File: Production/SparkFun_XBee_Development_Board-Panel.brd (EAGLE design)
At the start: 198.1 x 158.2 mm, 1094 parts, among them J1 USB Female Type C Connector, J13 QWIIC_RIGHT_ANGLE, J14 USB Female Type C Connector, J17 USB Female Type C Connector, J23 QWIIC_RIGHT_ANGLE, J24 USB Female Type C Connector, J27 USB Female Type C Connector, J3 USB Female Type C Connector, J33 QWIIC_RIGHT_ANGLE, J34 USB Female Type C Connector, J37 USB Female Type C Connector, J4 QWIIC_RIGHT_ANGLE, J43 QWIIC_RIGHT_ANGLE, J44 USB Female Type C Connector, J47 USB Female Type C Connector, J53 QWIIC_RIGHT_ANGLE, J54 USB Female Type C Connector, J57 USB Female Type C Connector, J63 QWIIC_RIGHT_ANGLE, J64 USB Female Type C Connector, J67 USB Female Type C Connector, J73 QWIIC_RIGHT_ANGLE, J74 USB Female Type C Connector, J77 USB Female Type C Connector, Q1 3.1A/30V/105mΩ, Q2 3.1A/30V/105mΩ, Q3 3.1A/30V/105mΩ, Q4 3.1A/30V/105mΩ, Q5 3.1A/30V/105mΩ, Q6 3.1A/30V/105mΩ, Q7 3.1A/30V/105mΩ, Q8 3.1A/30V/105mΩ, U1 FSUSB30MUX_MSOP10, U10 FT231XS, U11 FSUSB30MUX_MSOP10, U12 AP63203, U13 ESD Diode, U14 ESD Diode, U15 FT231XS, U16 FSUSB30MUX_MSOP10, U17 AP63203, U18 ESD Diode, U19 ESD Diode, U2 AP63203, U20 FT231XS, U21 FSUSB30MUX_MSOP10, U22 AP63203, U23 ESD Diode, U24 ESD Diode, U25 FT231XS, U26 FSUSB30MUX_MSOP10, U27 AP63203, U28 ESD Diode, U29 ESD Diode, U3 ESD Diode, U30 FT231XS, U31 FSUSB30MUX_MSOP10, U32 AP63203, U33 ESD Diode, U34 ESD Diode, U35 FT231XS, U36 FSUSB30MUX_MSOP10, U37 AP63203, U38 ESD Diode, U39 ESD Diode, U4 FSUSB30MUX_MSOP10, U40 FT231XS, U5 ESD Diode, U6 AP63203, U7 FT231XS, U8 ESD Diode, U9 ESD Diode

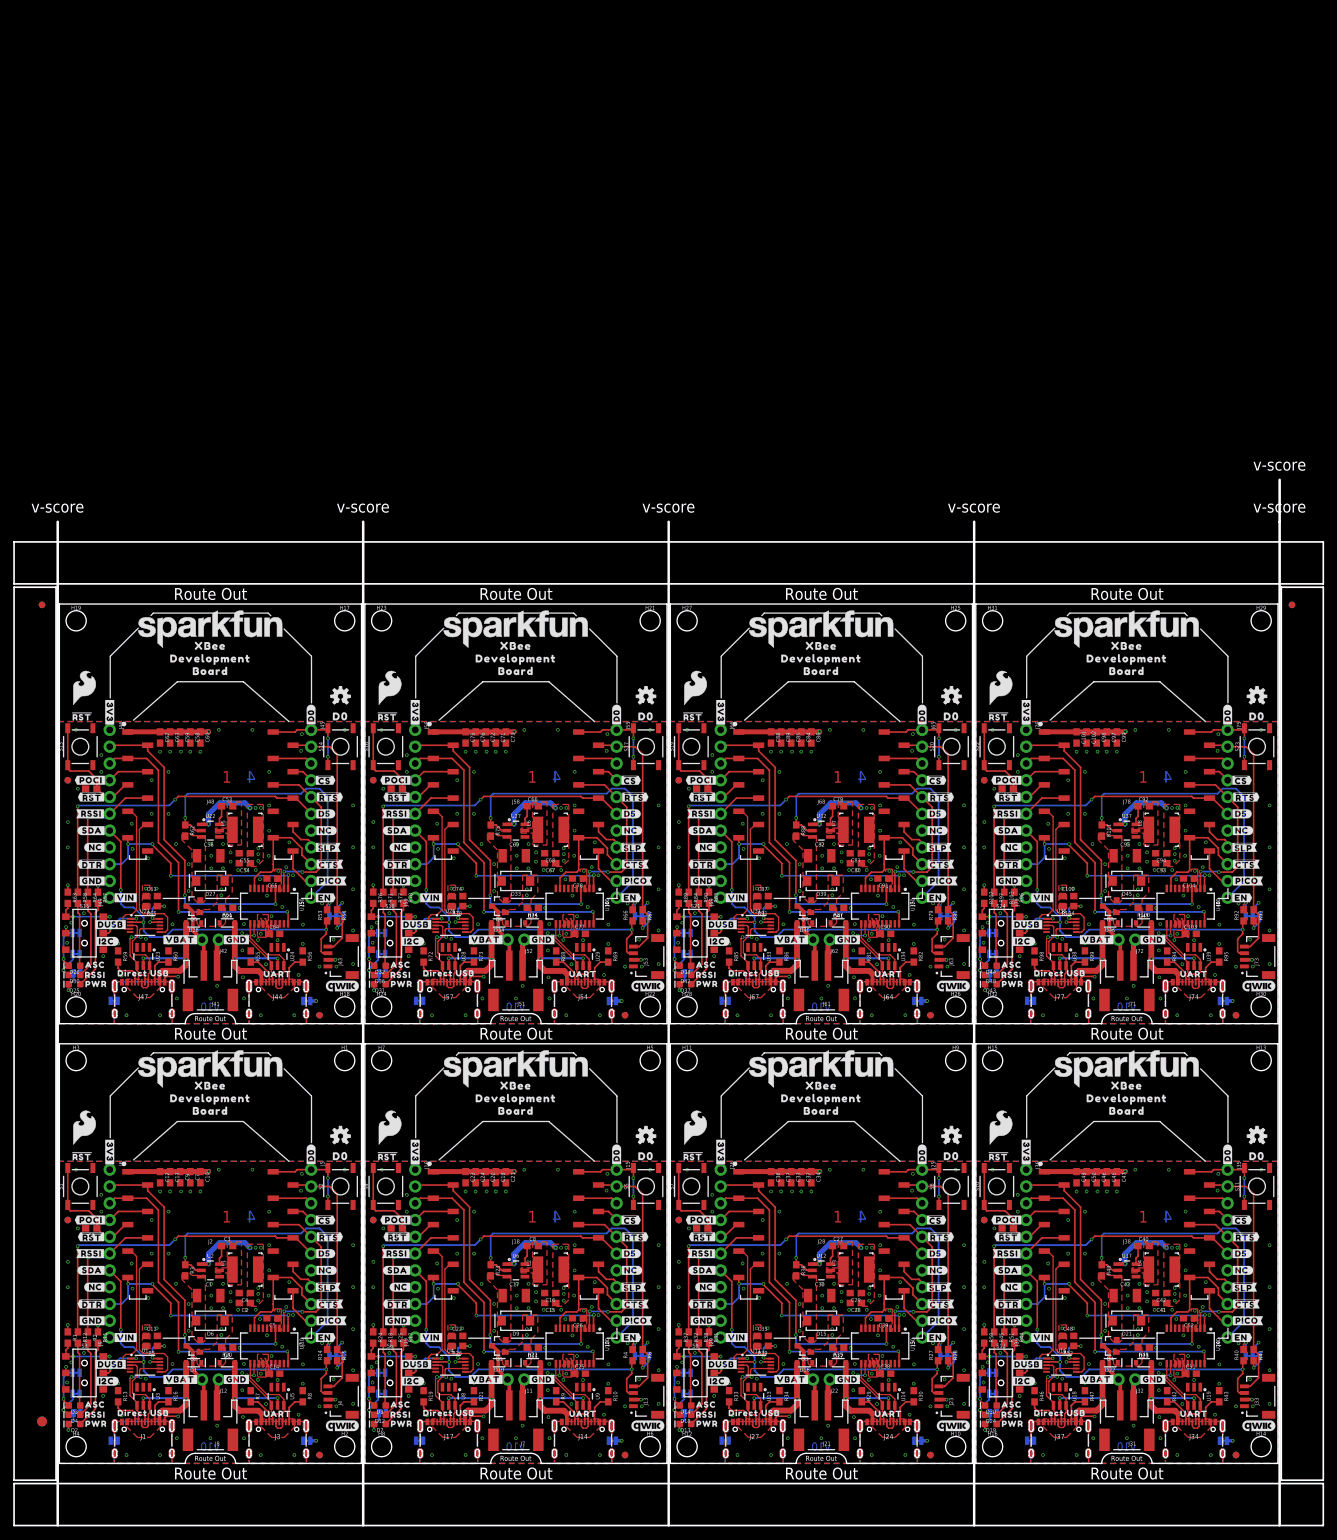
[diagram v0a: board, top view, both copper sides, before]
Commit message: Adds new 2 x 3 panel
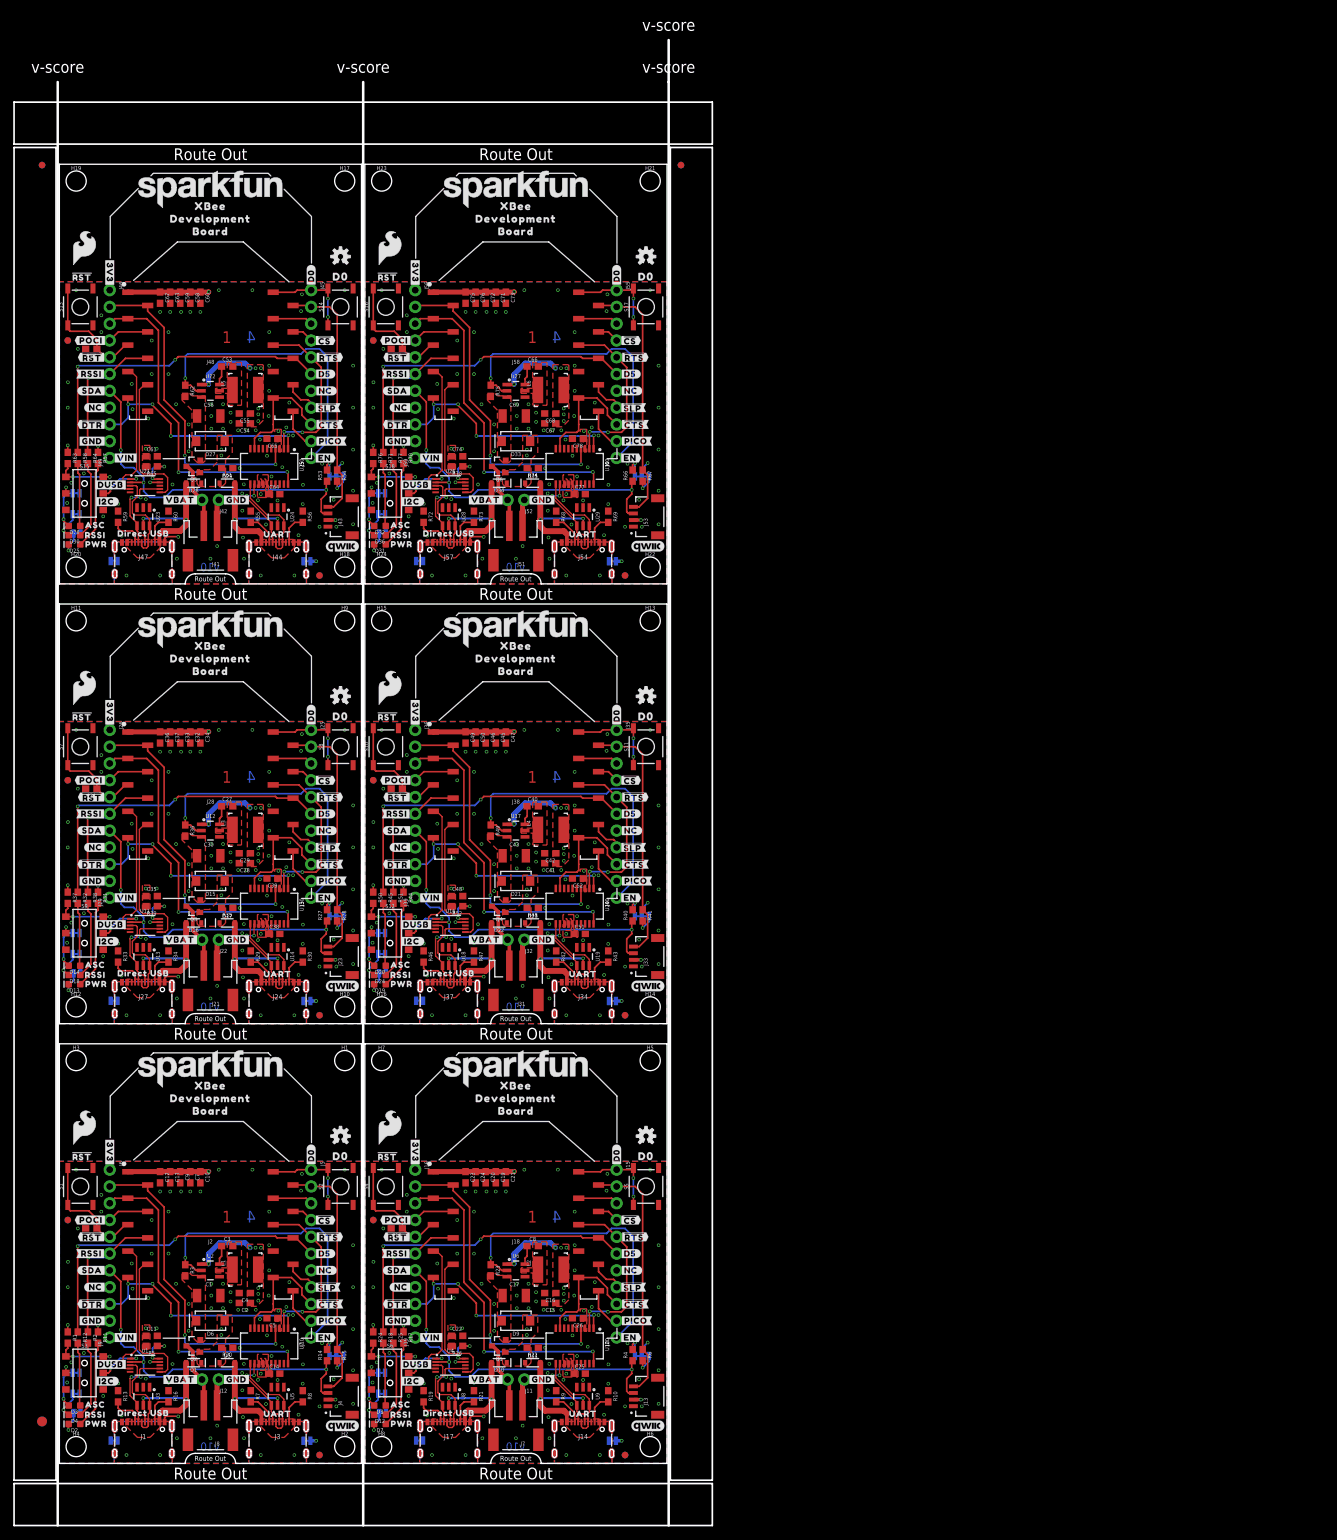
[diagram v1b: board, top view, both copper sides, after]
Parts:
- removed ALED6, ALED7, PLED6, PLED7, RLED6, RLED7, SHLD12, SHLD13, SHLD14, SHLD15: JUMPER-SMT_2_NC_TRACE_SILK, SparkFun-Jumpers:SMT-JUMPER_2_NC_TRACE_SILK
- removed C100, C103, C104, C79, C85, C87, C90, C91, C92, C98: 0.1uF, SparkFun-Capacitors:0603
- removed C101, C88: 10pF, SparkFun-Capacitors:0603
- removed C102, C89: 47pF, SparkFun-Capacitors:0603
- removed C80, C81, C93, C94: 22uF, SparkFun-Capacitors:0603
- removed C82, C95: 10uF, SparkFun-Capacitors:1210
- removed C83, C84, C96, C97: 10nF, SparkFun-Capacitors:0603
- removed C86, C99: 10uF, SparkFun-Capacitors:0603
- removed D37, D43: RED, SparkFun-LED:LED-0603
- removed D38, D44: BLUE, SparkFun-LED:LED-0603
- removed D39, D45: 3A/40V/500mV, SparkFun-DiscreteSemi:SMA-DIODE
- removed D40, D41, D46, D47: 3A/10V/280mV, SparkFun-DiscreteSemi:SOD-323
- removed D42, D48: Yellow, SparkFun-LED:LED-0603
- removed FD25, FD26, FD27, FD28, FD29, FD30, FD31, FD32: FIDUCIAL1X2, SparkFun-Aesthetics:FIDUCIAL-1X2
- removed H25, H26, H27, H28, H29, H30, H31, H32: STAND-OFFTIGHT, SparkFun-Hardware:STAND-OFF-TIGHT
- removed I2C_PU6, I2C_PU7: JUMPER-SMT_3_2-NC_TRACE_SILK, SparkFun-Jumpers:SMT-JUMPER_3_2-NC_TRACE_SILK
- removed J61, J71: (no value), SparkFun-Connectors:JST-2-SMD
- removed J62, J72: (no value), SparkFun-Connectors:1X02_NO_SILK
- removed J63, J73: QWIIC_RIGHT_ANGLE, SparkFun-Connectors:JST04_1MM_RA
- removed J64, J67, J74, J77: USB Female Type C Connector, SparkFun-Connectors:USB-C-16P-4LAYER-ISOLATED
- removed J65, J66, J75, J76: (no value), SparkFun-Connectors:1X10_NO_SILK
- removed J68, J78: (no value), xbee_smart_modem:XBEE3-SMD
- removed J69, J70, J79, J80: (no value), SparkFun-Connectors:1X01_NO_SILK_STAND
- removed L7, L8: 3.9UH, SparkFun-Coils:INDUCTOR_3.9UH
- removed LOGO19, LOGO22: OSHW-LOGOS, SparkFun-Aesthetics:OSHW-LOGO-S
- removed LOGO20, LOGO23: QWIIC_LOGO_5MM, SparkFun-Aesthetics:QWIIC_5MM
- removed LOGO21, LOGO24: SFE_LOGO_NAME.2_INCH, SparkFun-Aesthetics:SFE_LOGO_NAME_.2
- removed Q7, Q8: 3.1A/30V/105mΩ, SparkFun-DiscreteSemi:SOT23-3
- removed R100, R101, R87, R88: 10k, SparkFun-Resistors:0603
- removed R102, R89: 100k, SparkFun-Resistors:0603
- removed R103, R79, R80, R84, R90, R92, R93, R97: 2.2k, SparkFun-Resistors:0603
- removed R104, R91: 100, SparkFun-Resistors:0603
- removed R81, R82, R85, R86, R94, R95, R98, R99: 5.1k, SparkFun-Resistors:0603
- removed R83, R96: 1k, SparkFun-Resistors:0603
- removed S19, S20, S22, S23: (no value), SparkFun-Switches:TACTILE_SWITCH_SMD_5.2MM
- removed S21, S24: (no value), SparkFun-Switches:SWITCH_DPDT_SMD_AYZ0202
- removed U$403, U$470: (no value), top:##CS##19
- removed U$404, U$471: (no value), top:##CTS##25
- removed U$405, U$472: (no value), top:##RTS##24
- removed U$406, U$419, U$473, U$486: (no value), top:#3V3#1
- removed U$407, U$474: (no value), top:#D0#18
- removed U$408, U$415, U$420, U$442, U$475, U$482, U$487, U$509: (no value), top:#GND#0
- removed U$409, U$476: (no value), top:#I2C#33
- removed U$410, U$477: (no value), top:#PICO#23
- removed U$411, U$478: (no value), top:#RSSI#16
- removed U$412, U$479: (no value), top:#SDA#7
- removed U$413, U$480: (no value), top:#SHLD#30
- removed U$414, U$481: (no value), top:#SHLD1#31
- removed U$416, U$483: (no value), bot:#D5#3
- removed U$417, U$421, U$484, U$488: (no value), top:#VIN#4
- removed U$418, U$485: (no value), top:PWR26
- removed U$422, U$489: (no value), top:##SLP##27
- removed U$423, U$490: (no value), bot:#I2C#31
- removed U$424, U$491: (no value), bot:D03
- removed U$425, U$438, U$492, U$505: (no value), top:##RST##15
- removed U$426, U$441, U$493, U$508: (no value), top:#VBAT#5
- removed U$427, U$494: (no value), top:#ALED#21
- removed U$428, U$495: (no value), top:#PLED#20
- removed U$429, U$496: (no value), top:#D0#AD0#18
- removed U$430, U$497: (no value), top:#D3#AD3#22
- removed U$431, U$498: (no value), top:#D4#PICO#24
- removed U$432, U$499: (no value), top:#D5#ASSOC#24
- removed U$433, U$500: (no value), top:#D6##RTS##24
- removed U$434, U$501: (no value), top:#D7##CTS##25
- removed U$435, U$502: (no value), top:#D9##SLP##27
- removed U$436, U$503: (no value), top:#TXO#D13#13
- removed U$437, U$504: (no value), top:#RXI#D14#15
- removed U$439, U$506: (no value), top:#RSSI#D10#17
- removed U$440, U$507: (no value), top:#SDA#D11#8
- removed U$443, U$510: (no value), top:UART32
- removed U$444, U$511: (no value), top:#RST#30
- removed U$445, U$512: (no value), SparkFun-Aesthetics:SFE_LOGO_NAME_.2
- removed U$446, U$513: (no value), SparkFun-Aesthetics:SFE_LOGO_FLAME_.2
- removed U$447, U$514: (no value), top:RSSI31
- removed U$448, U$515: (no value), top:#RLED#22
- removed U$449, U$516: (no value), top:#POCI#D12#24
- removed U$450, U$517: (no value), top:#POCI#23
- removed U$451, U$518: (no value), top:##DTR##27
- removed U$452, U$453, U$519, U$520: (no value), topmirror:#EN#17
- removed U$454, U$457, U$521, U$524: (no value), topmirror:#NC#1
- removed U$455, U$456, U$522, U$523: (no value), botmirror:#NC#3
- removed U$458, U$525: (no value), topmirror:DIRECT_USB33
- removed U$459, U$461, U$526, U$528: (no value), topmirror:DEVELOPMENT1345
- removed U$460, U$462, U$527, U$529: (no value), topmirror:BOARD1346
- removed U$463, U$530: (no value), botmirror:#DUSB#31
- removed U$464, U$465, U$531, U$532: (no value), top:XBEE339
- removed U$466, U$533: (no value), top:#D1#AD1#SCL#8
- removed U$467, U$534: (no value), top:#D8##DTR##27
- removed U$468, U$535: (no value), top:ASC32
- removed U$469, U$536: (no value), top:#D2#AD2#SCLK#19
- removed U31, U36: FSUSB30MUX_MSOP10, SparkFun-IC-Special-Function:MSOP10
- removed U32, U37: AP63203, SparkFun-IC-Power:SOT23-6
- removed U33, U34, U38, U39: ESD Diode, SparkFun-DiscreteSemi:SOT-23-6
- removed U35, U40: FT231XS, SparkFun-IC-Comms:SSOP20_L
- moved C47 113.9 mm to (67.6, 109.9)
- moved C50 113.9 mm to (63.0, 109.9)
- moved D21 113.9 mm to (69.1, 88.1)
- moved E$3 113.9 mm to (94.1, 196.5)
- moved E$4 113.9 mm to (94.1, 196.5)
- moved FD13 113.9 mm to (47.5, 103.4)
- moved FD14 113.9 mm to (47.5, 103.4)
- moved I2C_PU2 113.9 mm to (41.9, 82.8)
- moved J25 113.9 mm to (38.1, 111.0)
- moved J30 113.9 mm to (38.1, 85.6)
- moved J31 113.9 mm to (69.1, 71.6)
- moved J33 113.9 mm to (86.9, 76.7)
- moved J38 113.9 mm to (69.1, 99.6)
- moved LOGO10 113.9 mm to (88.8, 116.1)
- moved LOGO12 113.9 mm to (69.1, 126.2)
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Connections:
- removed net !RESET!6: C83.1, J66.5, J68.5, S19.1, S19.2
- removed net !RESET!7: C96.1, J76.5, J78.5, S22.1, S22.2
- removed net 3.3V6: C80.1, C81.1, C84.1, C85.1, C86.1, C87.1, C88.1, C89.1, C90.1, C91.1, I2C_PU6.2, J63.2, J66.1, J68.1, L7.P$2, R83.1, R89.1, R91.2, U32.1, U35.13, U35.14, U35.15, U35.3
- removed net 3.3V7: C100.1, C101.1, C102.1, C103.1, C104.1, C93.1, C94.1, C97.1, C98.1, C99.1, I2C_PU7.2, J73.2, J76.1, J78.1, L8.P$2, R102.1, R104.2, R96.1, U37.1, U40.13, U40.14, U40.15, U40.3
- removed net ALED6: ALED6.2, D38.C
- removed net ALED7: ALED7.2, D44.C
- removed net D+6: J64.A6, J64.B6, U34.6, U35.11
- removed net D+7: J74.A6, J74.B6, U39.6, U40.11
- removed net D-6: J64.A7, J64.B7, U34.4, U35.12
- removed net D-7: J74.A7, J74.B7, U39.4, U40.12
- removed net D1/SCL6: J63.4, J65.2, J68.19, R80.1
- removed net D1/SCL7: J73.4, J75.2, J78.19, R93.1
- removed net D10/RSSI_PWM6: J66.6, J68.6, R90.1
- removed net D10/RSSI_PWM7: J76.6, J78.6, R103.1
- removed net D11/SDA6: J63.3, J66.7, R79.1, U31.2
- removed net D11/SDA7: J73.3, J76.7, R92.1, U36.2
- removed net D12/SPI_POCI6: J66.4, J68.4
- removed net D12/SPI_POCI7: J76.4, J78.4
- removed net D13/TXO6: J66.2, J68.2, U35.4
- removed net D13/TXO7: J76.2, J78.2, U40.4
- removed net D14/RXI6: J66.3, J68.3, U35.20
- removed net D14/RXI7: J76.3, J78.3, U40.20
- removed net D2/SPI_CLK6: J65.3, J68.18
- removed net D2/SPI_CLK7: J75.3, J78.18
- removed net D3/SPI_!CS!6: J65.4, J68.17
- removed net D3/SPI_!CS!7: J75.4, J78.17
- removed net D4/SPI_PICO6: J65.10, J68.11
- removed net D4/SPI_PICO7: J75.10, J78.11
- removed net D5/ASSOCIATE6: J65.6, J68.15, R84.1
- removed net D5/ASSOCIATE7: J75.6, J78.15, R97.1
- removed net D6: J65.1, J68.20, S20.1, S20.2
- removed net D6/!RTS!6: J65.5, J68.16, U35.2
- removed net D6/!RTS!7: J75.5, J78.16, U40.2
- removed net D7: J75.1, J78.20, S23.1, S23.2
- removed net D7/!CTS!6: J65.9, J68.12, U35.9
- removed net D7/!CTS!7: J75.9, J78.12, U40.9
- removed net D8/!DTR!6: J66.9, J68.9, U35.1
- removed net D8/!DTR!7: J76.9, J78.9, U40.1
- removed net D9/!SLEEP!6: J65.8, J68.13
- removed net D9/!SLEEP!7: J75.8, J78.13
- removed net DIRECT_D+6: J67.A6, J67.B6, U31.3, U33.6
- removed net DIRECT_D+7: J77.A6, J77.B6, U36.3, U38.6
- removed net DIRECT_D-6: J67.A7, J67.B7, U31.7, U33.4
- removed net DIRECT_D-7: J77.A7, J77.B7, U36.7, U38.4
- removed net DIRECT_SELECT6: S21.2, S21.5, U31.1
- removed net DIRECT_SELECT7: S24.2, S24.5, U36.1
- removed net EN6: J70.1, R88.1, U32.2
- removed net EN7: J80.1, R101.1, U37.2
- removed net FIRMWARE6: R89.2, S21.1, S21.4
- removed net FIRMWARE7: R102.2, S24.1, S24.4
- removed net GND6: ALED6.1, C80.2, C81.2, C82.2, C83.2, C84.2, C85.2, C86.2, C87.2, C88.2, C89.2, C90.2, C91.2, J61.1, J62.1, J63.1, J64.GND, J64.GND2, J66.10, J67.GND, J67.GND2, J68.10, PLED6.1, R81.1, R82.1, R85.1, R86.1, R87.1, RLED6.1, S19.3, S19.4, S20.3, S20.4, S21.3, S21.6, SHLD12.1, SHLD13.1, U31.5, U31.9, U32.4, U33.2, U34.2, U35.16, U35.6
- removed net GND7: ALED7.1, C100.2, C101.2, C102.2, C103.2, C104.2, C93.2, C94.2, C95.2, C96.2, C97.2, C98.2, C99.2, J71.1, J72.1, J73.1, J74.GND, J74.GND2, J76.10, J77.GND, J77.GND2, J78.10, PLED7.1, R100.1, R94.1, R95.1, R98.1, R99.1, RLED7.1, S22.3, S22.4, S23.3, S23.4, S24.3, S24.6, SHLD14.1, SHLD15.1, U36.5, U36.9, U37.4, U38.2, U39.2, U40.16, U40.6
- removed net N$100: C95.1, D45.C, Q8.2, R101.2, U37.3
- removed net N$101: C92.1, U37.6
- removed net N$102: C92.2, L8.P$1, U37.5
- removed net N$103: D48.A, R103.2
- removed net N$104: R104.1, U36.10
- removed net N$79: I2C_PU6.3, R79.2
- removed net N$80: I2C_PU6.1, R80.2
- removed net N$81: J64.B5, R82.2
- removed net N$82: J64.A5, R81.2
- removed net N$83: D37.A, R83.2
- removed net N$84: D38.A, R84.2
- removed net N$85: J67.B5, R86.2
- removed net N$86: J67.A5, R85.2
- removed net N$87: C82.1, D39.C, Q7.2, R88.2, U32.3
- removed net N$88: C79.1, U32.6
- removed net N$89: C79.2, L7.P$1, U32.5
- removed net N$90: D42.A, R90.2
- removed net N$91: R91.1, U31.10
- removed net N$92: I2C_PU7.3, R92.2
- removed net N$93: I2C_PU7.1, R93.2
- removed net N$94: J74.B5, R95.2
- removed net N$95: J74.A5, R94.2
- removed net N$96: D43.A, R96.2
- removed net N$97: D44.A, R97.2
- removed net N$98: J77.B5, R99.2
- removed net N$99: J77.A5, R98.2
- removed net PLED6: D37.C, PLED6.2
- removed net PLED7: D43.C, PLED7.2
- removed net RLED6: D42.C, RLED6.2
- removed net RLED7: D48.C, RLED7.2
- removed net SHLD12: J64.SHLD1, J64.SHLD2, J64.SHLD3, J64.SHLD4, J64.SHLD5, J64.SHLD6, J64.SHLD7, J64.SHLD8, SHLD12.2
- removed net SHLD13: J67.SHLD1, J67.SHLD2, J67.SHLD3, J67.SHLD4, J67.SHLD5, J67.SHLD6, J67.SHLD7, J67.SHLD8, SHLD13.2
- removed net SHLD14: J74.SHLD1, J74.SHLD2, J74.SHLD3, J74.SHLD4, J74.SHLD5, J74.SHLD6, J74.SHLD7, J74.SHLD8, SHLD14.2
- removed net SHLD15: J77.SHLD1, J77.SHLD2, J77.SHLD3, J77.SHLD4, J77.SHLD5, J77.SHLD6, J77.SHLD7, J77.SHLD8, SHLD15.2
- removed net VIN6: D39.A, D40.C, D41.C, J69.1, Q7.1, R87.2
- removed net VIN7: D45.A, D46.C, D47.C, J79.1, Q8.1, R100.2
- removed net V_BATT6: J61.2, J62.2, Q7.3
- removed net V_BATT7: J71.2, J72.2, Q8.3
- removed net V_USB6: D41.A, J64.VBUS1, J64.VBUS2, U34.5
- removed net V_USB7: D47.A, J74.VBUS1, J74.VBUS2, U39.5
- removed net V_USB_7: D40.A, J67.VBUS1, J67.VBUS2, U33.5
- removed net V_USB_8: D46.A, J77.VBUS1, J77.VBUS2, U38.5
- removed net XBEE_D+/SDA6: J68.7, U31.4
- removed net XBEE_D+/SDA7: J78.7, U36.4
- removed net XBEE_D-6: J68.8, U31.6
- removed net XBEE_D-7: J78.8, U36.6
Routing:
- net D11/SDA7: track 54.8 -> 0.00 mm, vias 3 -> 0
- net D11/SDA6: track 54.8 -> 0.00 mm, vias 3 -> 0
- net D5/ASSOCIATE6: track 50.1 -> 0.00 mm, vias 2 -> 0
- net D5/ASSOCIATE7: track 50.1 -> 0.00 mm, vias 2 -> 0
- net D14/RXI7: track 49.5 -> 0.00 mm, vias 2 -> 0
- net D14/RXI6: track 49.5 -> 0.00 mm, vias 2 -> 0
- net D13/TXO7: track 48.2 -> 0.00 mm, vias 2 -> 0
- net D13/TXO6: track 48.2 -> 0.00 mm, vias 2 -> 0
- net EN7: track 46.0 -> 0.00 mm, vias 1 -> 0
- net EN6: track 46.0 -> 0.00 mm, vias 1 -> 0
- net D1/SCL6: track 38.1 -> 0.00 mm
- net D1/SCL7: track 38.1 -> 0.00 mm
- net D8/!DTR!6: track 35.7 -> 0.00 mm, vias 4 -> 0
- net D8/!DTR!7: track 35.7 -> 0.00 mm, vias 4 -> 0
- net 3.3V6: track 27.8 -> 0.00 mm, vias 15 -> 0
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- removed copper zone on layer 1, net 3.3V6
- removed copper zone on layer 15, net 3.3V6
- removed copper zone on layer 1, net 3.3V7
- removed copper zone on layer 15, net 3.3V7
- removed copper zone on layer 1, net GND6
- removed copper zone on layer 16, net GND6
- removed copper zone on layer 2, net GND6
- removed copper zone on layer 1, net GND7
- removed copper zone on layer 16, net GND7
- removed copper zone on layer 2, net GND7
- removed copper zone on layer 1, net N$100
- removed copper zone on layer 1, net N$102
- removed copper zone on layer 1, net N$87
- removed copper zone on layer 1, net N$89
- removed copper zone on layer 1, net SHLD12
- removed copper zone on layer 15, net SHLD12
- removed copper zone on layer 16, net SHLD12
- removed copper zone on layer 2, net SHLD12
- removed copper zone on layer 1, net SHLD13
- removed copper zone on layer 15, net SHLD13
- removed copper zone on layer 16, net SHLD13
- removed copper zone on layer 2, net SHLD13
- removed copper zone on layer 1, net SHLD14
- removed copper zone on layer 15, net SHLD14
- removed copper zone on layer 16, net SHLD14
- removed copper zone on layer 2, net SHLD14
- removed copper zone on layer 1, net SHLD15
- removed copper zone on layer 15, net SHLD15
- removed copper zone on layer 16, net SHLD15
- removed copper zone on layer 2, net SHLD15
- removed copper zone on layer 1, net VIN6
- removed copper zone on layer 1, net VIN7
- removed copper zone on layer 1, net V_USB6
- removed copper zone on layer 1, net V_USB7
- removed copper zone on layer 1, net V_USB_7
- removed copper zone on layer 1, net V_USB_8
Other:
- board size 198.1 x 158.2 mm -> 105.7 x 224.8 mm
